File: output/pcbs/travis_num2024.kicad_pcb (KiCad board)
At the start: 2 copper layers, 85.2 x 132.8 mm, 92 parts

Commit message: numpad routed, with outputs
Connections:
- ROT1 pad 1: col4 -> col3
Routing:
- added copper zone on B.Cu, net GND
- added copper zone on F.Cu, net GND
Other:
- board text added: "2024.04.13"
- board text removed: "2024.04.10"
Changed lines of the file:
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@@
   (title_block
     (title "travis_num2024")
-    (rev "2024.04.10")
+    (rev "2024.04.13")
     (company "Travis Hardiman")
   )
@@
 (net 59 "matrix_col3_row2")
 (net 60 "matrix_col3_row4")
-(net 61 "col4")
-(net 62 "enc_to")
+(net 61 "enc_to")
   (net_class Default "This is the default net class."
     (clearance 0.2)
@@
 (add_net "matrix_col3_row2")
 (add_net "matrix_col3_row4")
-(add_net "col4")
 (add_net "enc_to")
   )
@@
             (pad C thru_hole circle (at -7.62 -0.04) (size 2 2) (drill 1) (layers *.Cu *.Mask) (net 12 "encC"))
             (pad B thru_hole circle (at -7.62 2.46) (size 2 2) (drill 1) (layers *.Cu *.Mask) (net 3 "GND"))
-            (pad 1 thru_hole circle (at 6.88 -2.54) (size 1.5 1.5) (drill 1) (layers *.Cu *.Mask) (net 61 "col4"))
-            (pad 2 thru_hole circle (at 6.88 2.46) (size 1.5 1.5) (drill 1) (layers *.Cu *.Mask) (net 62 "enc_to"))
+            (pad 1 thru_hole circle (at 6.88 -2.54) (size 1.5 1.5) (drill 1) (layers *.Cu *.Mask) (net 16 "col3"))
+            (pad 2 thru_hole circle (at 6.88 2.46) (size 1.5 1.5) (drill 1) (layers *.Cu *.Mask) (net 61 "enc_to"))
             (pad "" thru_hole rect (at -0.12 -5.64 -90) (size 3.2 2) (drill oval 2.8 1.5) (layers *.Cu *.Mask))
             (pad "" thru_hole rect (at -0.12 5.56 -90)  (size 3.2 2) (drill oval 2.8 1.5) (layers *.Cu *.Mask))
@@
       (stroke (width 0.1) (type solid)) (layer "B.Fab") )
     (pad 1 thru_hole rect (at 0 0 -90) (size 1.6 1.6) (drill 0.8) (layers "*.Cu" "*.Mask") (net 10 "row4"))
-    (pad 2 thru_hole oval (at 7.62 0 -90) (size 1.6 1.6) (drill 0.8) (layers "*.Cu" "*.Mask") (net 62 "enc_to"))
+    (pad 2 thru_hole oval (at 7.62 0 -90) (size 1.6 1.6) (drill 0.8) (layers "*.Cu" "*.Mask") (net 61 "enc_to"))
     (model "${SCOTTOKEEBS_KICAD}/3dmodels/ScottoKeebs_Components.3dshapes/Diode_DO-35.step"
       (offset (xyz 0 0 0))
@@
           )
       )
-      (gr_text "2024.04.10"
+      (gr_text "2024.04.13"
         (at 104.91250000000001 85.43749999999997 0)
         (layer F.SilkS)
@@
           )
       )
+    (zone
+      (net 3)
+      (net_name "GND")
+      (locked no)
+      (layers "B.Cu")
+      (name "back ground")
+      (hatch edge 0.5)
+      (connect_pads
+        (clearance 0.508)
+      )
+      (min_thickness 0.25)
+      (filled_areas_thickness no)
+      (fill
+        yes
+        (thermal_gap 0.5)
+        (thermal_bridge_width 0.5)
+        (smoothing chamfer)
+        (radius 0.5)
+        (island_removal_mode 1)
+        (island_area_min 5)
+      )
+      (polygon
+        (pts
+          (xy 0 0) (xy 420 0) (xy 420 297) (xy 0 297)
+        )
+      )
+    )
+    (zone
+      (net 3)
+      (net_name "GND")
+      (locked no)
+      (layers "F.Cu")
+      (name "fore ground")
+      (hatch edge 0.5)
+      (connect_pads yes
+        (clearance 0.508)
+      )
+      (min_thickness 0.25)
+      (filled_areas_thickness no)
+      (fill
+        (mode hatch)
+        (thermal_gap 0.5)
+        (thermal_bridge_width 0.5)
+        (smoothing chamfer)
+        (radius 0.5)
+        (island_removal_mode 1)
+        (island_area_min 5)
+        (hatch_thickness 1)
+        (hatch_gap 1.5)
+        (hatch_orientation 45)
+        (hatch_border_algorithm hatch_thickness)
+        (hatch_min_hole_area 0.3)
+      )
+      (polygon
+        (pts
+          (xy 0 0) (xy 420 0) (xy 420 297) (xy 0 297)
+        )
+      )
+    )
   (gr_line (start 27.474999999999998 207.525) (end 27.474999999999998 84.74999999999997) (angle 90) (layer Edge.Cuts) (width 0.15))
 (gr_line (start 32.474999999999994 79.74999999999997) (end 107.67500000000001 79.74999999999997) (angle 90) (layer Edge.Cuts) (width 0.15))

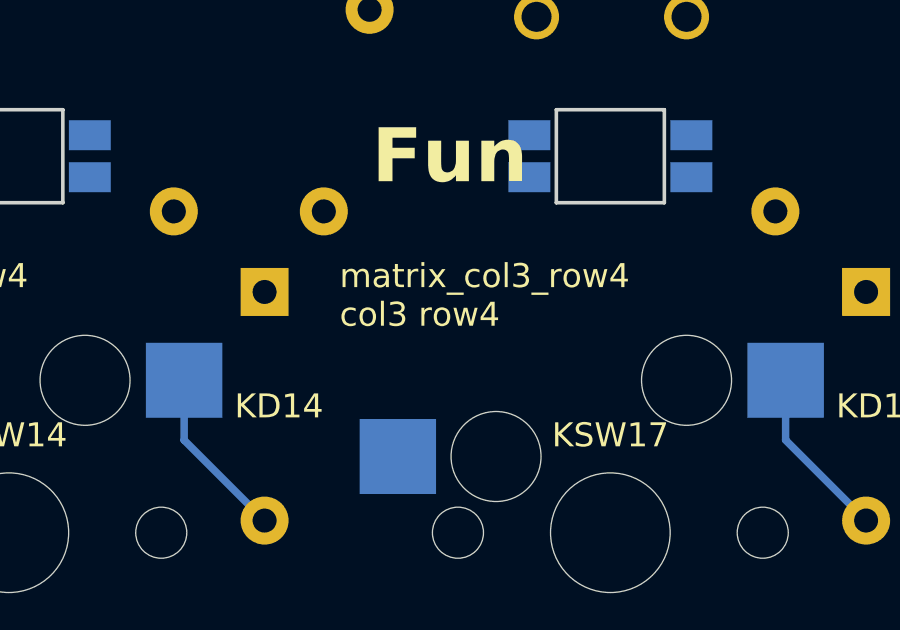
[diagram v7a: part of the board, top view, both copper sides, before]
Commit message: fixed rows, re-routed
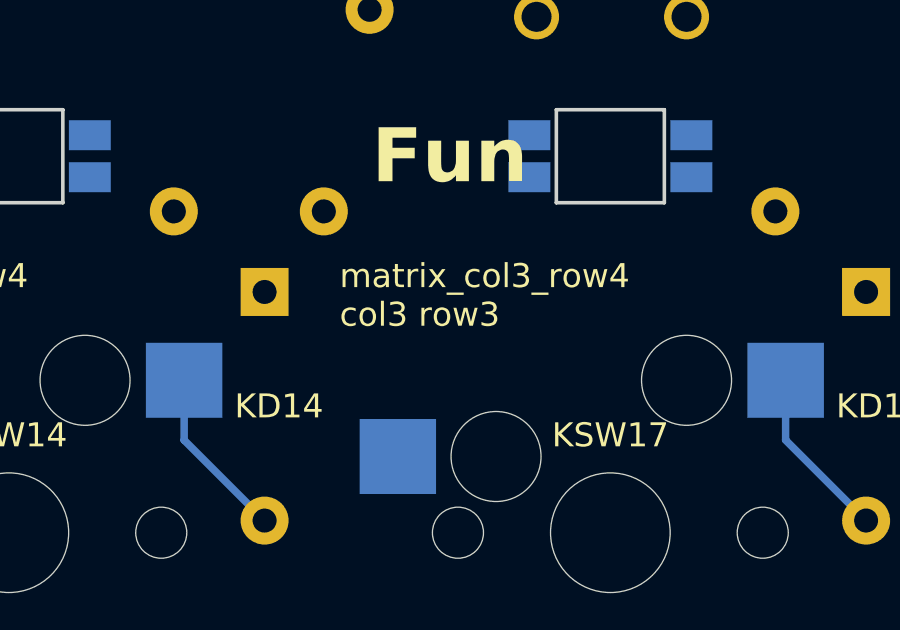
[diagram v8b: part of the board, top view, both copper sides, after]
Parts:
- removed KLED1, KLED10, KLED11, KLED12, KLED13, KLED14, KLED15, KLED16, KLED17, KLED2, KLED3, KLED4, KLED5, KLED6, KLED7, KLED8, KLED9: SK6812mini-e, travis:led_SK6812mini-e
- added LED_10-row3-col2: SK6812mini-e, travis:led_SK6812mini-e, B.Cu at (80.1, 144.8)
- added LED_11-row2-col3: SK6812mini-e, travis:led_SK6812mini-e, B.Cu at (105.1, 149.9)
- added LED_12-row2-col2: SK6812mini-e, travis:led_SK6812mini-e, B.Cu at (80.1, 164.9)
- added LED_13-row2-col1: SK6812mini-e, travis:led_SK6812mini-e, B.Cu at (60.0, 164.9)
- added LED_14-row2-col0: SK6812mini-e, travis:led_SK6812mini-e, B.Cu at (40.0, 164.9)
- added LED_15-row1-col0: SK6812mini-e, travis:led_SK6812mini-e, B.Cu at (40.0, 184.9)
- added LED_16-row1-col1: SK6812mini-e, travis:led_SK6812mini-e, B.Cu at (60.0, 184.9)
- added LED_17-row1-col2: SK6812mini-e, travis:led_SK6812mini-e, B.Cu at (80.1, 184.9)
- added LED_18-row0-col3: SK6812mini-e, travis:led_SK6812mini-e, B.Cu at (105.1, 190.0)
- added LED_19-row0-col2: SK6812mini-e, travis:led_SK6812mini-e, B.Cu at (80.1, 205.0)
- added LED_20-row0-col0: SK6812mini-e, travis:led_SK6812mini-e, B.Cu at (50.0, 205.0)
- added LED_4-row3-col3: SK6812mini-e, travis:led_SK6812mini-e, B.Cu at (100.2, 124.8)
- added LED_5-row4-col2: SK6812mini-e, travis:led_SK6812mini-e, B.Cu at (80.1, 124.8)
- added LED_6-row4-col1: SK6812mini-e, travis:led_SK6812mini-e, B.Cu at (60.0, 124.8)
- added LED_7-row4-col0: SK6812mini-e, travis:led_SK6812mini-e, B.Cu at (40.0, 124.8)
- added LED_8-row3-col0: SK6812mini-e, travis:led_SK6812mini-e, B.Cu at (40.0, 144.8)
- added LED_9-row3-col1: SK6812mini-e, travis:led_SK6812mini-e, B.Cu at (60.0, 144.8)
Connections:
- KD17 pad 1: row4 -> row3
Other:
- board text added: "matrix_col3_row4 col3 row3"
- board text removed: "matrix_col3_row4 col3 row4"
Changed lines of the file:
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@@
   (layer B.Cu)
   (at 40.0000 184.9100 0)
-  (fp_text reference "KLED1" (at 0 -2.2 0) (layer B.SilkS)
+  (fp_text reference "LED_15-row1-col0" (at 0 -2.2 0) (layer B.SilkS) hide
     (effects (font (size 0.8 0.8) (thickness 0.15)) (justify mirror))
   )
@@
   (layer B.Cu)
   (at 40.0000 144.8100 0)
-  (fp_text reference "KLED2" (at 0 -2.2 0) (layer B.SilkS)
+  (fp_text reference "LED_8-row3-col0" (at 0 -2.2 0) (layer B.SilkS) hide
     (effects (font (size 0.8 0.8) (thickness 0.15)) (justify mirror))
   )
@@
   (layer B.Cu)
   (at 60.0500 184.9100 0)
-  (fp_text reference "KLED3" (at 0 -2.2 0) (layer B.SilkS)
+  (fp_text reference "LED_16-row1-col1" (at 0 -2.2 0) (layer B.SilkS) hide
     (effects (font (size 0.8 0.8) (thickness 0.15)) (justify mirror))
   )
@@
   (layer B.Cu)
   (at 60.0500 144.8100 0)
-  (fp_text reference "KLED4" (at 0 -2.2 0) (layer B.SilkS)
+  (fp_text reference "LED_9-row3-col1" (at 0 -2.2 0) (layer B.SilkS) hide
     (effects (font (size 0.8 0.8) (thickness 0.15)) (justify mirror))
   )
@@
   (layer B.Cu)
   (at 80.1000 184.9100 0)
-  (fp_text reference "KLED5" (at 0 -2.2 0) (layer B.SilkS)
+  (fp_text reference "LED_17-row1-col2" (at 0 -2.2 0) (layer B.SilkS) hide
     (effects (font (size 0.8 0.8) (thickness 0.15)) (justify mirror))
   )
@@
   (layer B.Cu)
   (at 80.1000 144.8100 0)
-  (fp_text reference "KLED6" (at 0 -2.2 0) (layer B.SilkS)
+  (fp_text reference "LED_10-row3-col2" (at 0 -2.2 0) (layer B.SilkS) hide
     (effects (font (size 0.8 0.8) (thickness 0.15)) (justify mirror))
   )
@@
   (layer B.Cu)
   (at 50.0250 204.9600 180)
-  (fp_text reference "KLED7" (at 0 2.2 0) (layer B.SilkS)
+  (fp_text reference "LED_20-row0-col0" (at 0 2.2 0) (layer B.SilkS) hide
     (effects (font (size 0.8 0.8) (thickness 0.15)) (justify mirror))
   )
@@
   (layer B.Cu)
   (at 40.0000 164.8600 180)
-  (fp_text reference "KLED8" (at 0 2.2 0) (layer B.SilkS)
+  (fp_text reference "LED_14-row2-col0" (at 0 2.2 0) (layer B.SilkS) hide
     (effects (font (size 0.8 0.8) (thickness 0.15)) (justify mirror))
   )
@@
   (layer B.Cu)
   (at 40.0000 124.7600 180)
-  (fp_text reference "KLED9" (at 0 2.2 0) (layer B.SilkS)
+  (fp_text reference "LED_7-row4-col0" (at 0 2.2 0) (layer B.SilkS) hide
     (effects (font (size 0.8 0.8) (thickness 0.15)) (justify mirror))
   )
@@
   (layer B.Cu)
   (at 60.0500 164.8600 180)
-  (fp_text reference "KLED10" (at 0 2.2 0) (layer B.SilkS)
+  (fp_text reference "LED_13-row2-col1" (at 0 2.2 0) (layer B.SilkS) hide
     (effects (font (size 0.8 0.8) (thickness 0.15)) (justify mirror))
   )
@@
   (layer B.Cu)
   (at 60.0500 124.7600 180)
-  (fp_text reference "KLED11" (at 0 2.2 0) (layer B.SilkS)
+  (fp_text reference "LED_6-row4-col1" (at 0 2.2 0) (layer B.SilkS) hide
     (effects (font (size 0.8 0.8) (thickness 0.15)) (justify mirror))
   )
@@
   (layer B.Cu)
   (at 80.1000 204.9600 180)
-  (fp_text reference "KLED12" (at 0 2.2 0) (layer B.SilkS)
+  (fp_text reference "LED_19-row0-col2" (at 0 2.2 0) (layer B.SilkS) hide
     (effects (font (size 0.8 0.8) (thickness 0.15)) (justify mirror))
   )
@@
   (layer B.Cu)
   (at 80.1000 164.8600 180)
-  (fp_text reference "KLED13" (at 0 2.2 0) (layer B.SilkS)
+  (fp_text reference "LED_12-row2-col2" (at 0 2.2 0) (layer B.SilkS) hide
     (effects (font (size 0.8 0.8) (thickness 0.15)) (justify mirror))
   )
@@
   (layer B.Cu)
   (at 80.1000 124.7600 180)
-  (fp_text reference "KLED14" (at 0 2.2 0) (layer B.SilkS)
+  (fp_text reference "LED_5-row4-col2" (at 0 2.2 0) (layer B.SilkS) hide
     (effects (font (size 0.8 0.8) (thickness 0.15)) (justify mirror))
   )
@@
   (layer B.Cu)
   (at 105.1100 189.9750 270)
-  (fp_text reference "KLED15" (at 0 2.2 90) (layer B.SilkS)
+  (fp_text reference "LED_18-row0-col3" (at 0 2.2 90) (layer B.SilkS) hide
     (effects (font (size 0.8 0.8) (thickness 0.15)) (justify mirror))
   )
@@
   (layer B.Cu)
   (at 105.1100 149.8750 270)
-  (fp_text reference "KLED16" (at 0 2.2 90) (layer B.SilkS)
+  (fp_text reference "LED_11-row2-col3" (at 0 2.2 90) (layer B.SilkS) hide
     (effects (font (size 0.8 0.8) (thickness 0.15)) (justify mirror))
   )
@@
     )
 )
-(gr_text "matrix_col3_row4\ncol3 row4" (at 91.1250 110.7750 0) (layer F.SilkS)
+(gr_text "matrix_col3_row4\ncol3 row3" (at 91.1250 110.7750 0) (layer F.SilkS)
   (effects (font (size 0.8 0.8) (thickness 0.15)) (justify top left))
 )
-(gr_text "matrix_col3_row4\ncol3 row4" (at 91.1250 110.7750  0) (layer B.SilkS)
+(gr_text "matrix_col3_row4\ncol3 row3" (at 91.1250 110.7750  0) (layer B.SilkS)
   (effects (font (size 0.8 0.8) (thickness 0.15)) (justify top right mirror))
 )
@@
   (fp_line (start 7.62 0) (end 5.81 0)
     (stroke (width 0.1) (type solid)) (layer "B.Fab") )
-  (pad 1 thru_hole rect (at 0 0 270) (size 1.6 1.6) (drill 0.8) (layers "*.Cu" "*.Mask") (net 10 "row4"))
+  (pad 1 thru_hole rect (at 0 0 270) (size 1.6 1.6) (drill 0.8) (layers "*.Cu" "*.Mask") (net 9 "row3"))
   (pad 2 thru_hole oval (at 7.62 0 270) (size 1.6 1.6) (drill 0.8) (layers "*.Cu" "*.Mask") (net 60 "matrix_col3_row4"))
   (model "${SCOTTOKEEBS_KICAD}/3dmodels/ScottoKeebs_Components.3dshapes/Diode_DO-35.step"
@@
   (layer B.Cu)
   (at 100.1500 124.7600 180)
-  (fp_text reference "KLED17" (at 0 2.2 0) (layer B.SilkS)
+  (fp_text reference "LED_4-row3-col3" (at 0 2.2 0) (layer B.SilkS) hide
     (effects (font (size 0.8 0.8) (thickness 0.15)) (justify mirror))
   )
